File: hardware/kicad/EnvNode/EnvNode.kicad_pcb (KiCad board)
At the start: 2 copper layers, 111 x 95 mm, 38 parts, among them J1 Conn_01x02_Pin, U1 LT1963AxST-3.3, U2 ESP32-DevKitC

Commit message: Changed Value to LM3940IMP
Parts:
- U1: value LT1963AxST-3.3 -> LM3940IMP-3.3/NOPB
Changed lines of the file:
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@@
 			)
 		)
-		(property "Value" "LT1963AxST-3.3"
+		(property "Value" "LM3940IMP-3.3/NOPB"
 			(at 0 4.5 90)
 			(layer "F.Fab")

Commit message: hardware(mainboard): add board ID EEPROM for revision 0.2
Add a 24AA025E48 EEPROM to the system I2C bus on GPIO21/22.
Configure address pins A0 and A1 for address 0x50 and update the
board revision markings to Rev 0.2.
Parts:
- added U3: 24AA025E-OT, Package_TO_SOT_SMD:SOT-23-6, F.Cu at (148.1, 45.7)
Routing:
- net +3V3: track 342.1 -> 358.9 mm
- net I2C0_SDA: track 129.8 -> 146.5 mm
- net I2C0_SCL: track 118.2 -> 129.3 mm
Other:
- board text added: "${TITLE} - Rev ${REVISION}"
- board text removed: "${TITLE} - ${REVISION}"

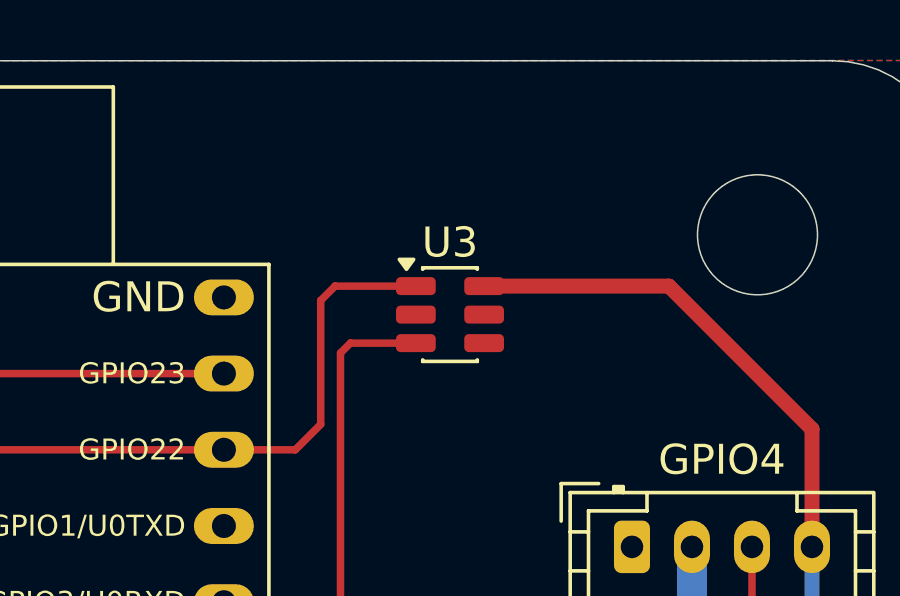
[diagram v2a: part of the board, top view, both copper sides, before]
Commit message: Change EEPROM-Package to SOT-23-6
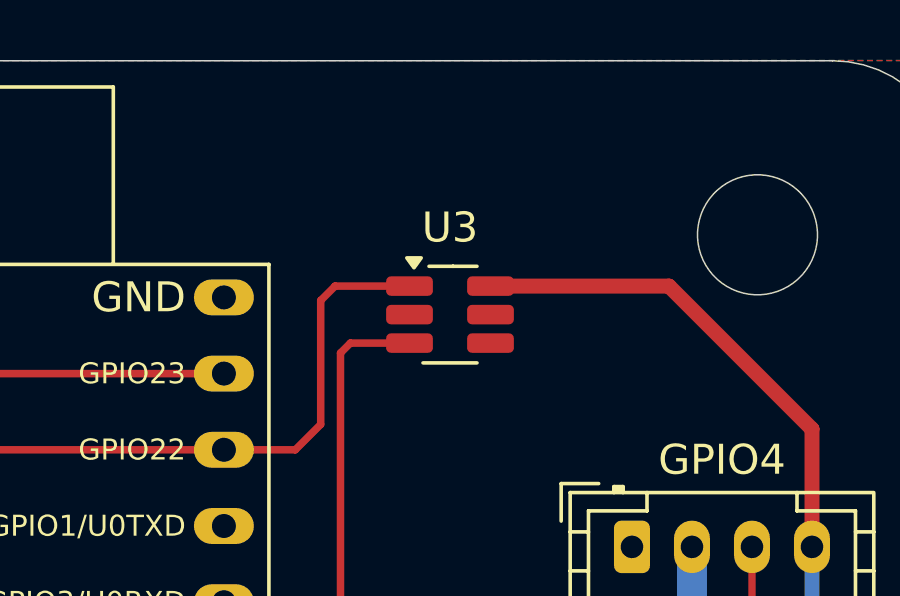
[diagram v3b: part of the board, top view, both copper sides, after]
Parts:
- U3: footprint Package_TO_SOT_SMD:SOT-23-6 -> Package_TO_SOT_SMD:SOT-23-6_Handsoldering
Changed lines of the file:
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@@
 		)
 	)
-	(footprint "Package_TO_SOT_SMD:SOT-23-6"
+	(footprint "Package_TO_SOT_SMD:SOT-23-6_Handsoldering"
 		(layer "F.Cu")
 		(at 148.09 45.7)
-		(descr "SOT, 6 Pin (JEDEC MO-178 Var AB https://www.jedec.org/document_search?search_api_views_fulltext=MO-178)")
-		(tags "SOT TO_SOT_SMD")
+		(descr "6-pin SOT-23 package, Handsoldering")
+		(tags "SOT-23-6 Handsoldering")
 		(property "Reference" "U3"
-			(at 0 -2.4 0)
+			(at 0 -2.9 0)
 			(layer "F.SilkS")
 			(effects
@@
 		)
 		(property "Value" "24AA025E-OT"
-			(at 0 2.4 0)
+			(at 0 2.9 0)
 			(layer "F.Fab")
 			(effects
@@
 		(property "Datasheet" "https://ww1.microchip.com/downloads/aemDocuments/documents/MPD/ProductDocuments/DataSheets/2-Kbit-I2C-Serial-EEPROMs-+EUI-48-or-EUI-64-Node-20002124.pdf"
 			(at 0 0 0)
+			(unlocked yes)
 			(layer "F.Fab")
 			(hide yes)
@@
 				(font
 					(size 1.27 1.27)
+					(thickness 0.15)
 				)
 			)
@@
 		(property "Description" "I2C Serial EEPROM with EUI-48 or EUI-64, 2Kb, SOT-23-6"
 			(at 0 0 0)
+			(unlocked yes)
 			(layer "F.Fab")
 			(hide yes)
@@
 				(font
 					(size 1.27 1.27)
-				)
-			)
-		)
-		(property "KiLib_Generator" "package/gullwing"
-			(at 0 0 0)
-			(layer "F.SilkS")
-			(hide yes)
-			(effects
-				(font
-					(size 1 1)
 					(thickness 0.15)
 				)
@@
 		(duplicate_pad_numbers_are_jumpers no)
 		(fp_line
-			(start -0.91 -1.56)
-			(end 0.91 -1.56)
-			(stroke
-				(width 0.12)
-				(type solid)
-			)
-			(layer "F.SilkS")
-		)
-		(fp_line
-			(start -0.91 -1.51)
-			(end -0.91 -1.56)
-			(stroke
-				(width 0.12)
-				(type solid)
-			)
-			(layer "F.SilkS")
-		)
-		(fp_line
-			(start -0.91 1.56)
-			(end -0.91 1.51)
-			(stroke
-				(width 0.12)
-				(type solid)
-			)
-			(layer "F.SilkS")
-		)
-		(fp_line
-			(start 0.91 -1.56)
-			(end 0.91 -1.51)
-			(stroke
-				(width 0.12)
-				(type solid)
-			)
-			(layer "F.SilkS")
-		)
-		(fp_line
-			(start 0.91 1.51)
-			(end 0.91 1.56)
-			(stroke
-				(width 0.12)
-				(type solid)
-			)
-			(layer "F.SilkS")
-		)
-		(fp_line
-			(start 0.91 1.56)
-			(end -0.91 1.56)
+			(start -0.9 1.61)
+			(end 0.9 1.61)
+			(stroke
+				(width 0.12)
+				(type solid)
+			)
+			(layer "F.SilkS")
+		)
+		(fp_line
+			(start 0.1 -1.61)
+			(end -0.7 -1.61)
+			(stroke
+				(width 0.12)
+				(type solid)
+			)
+			(layer "F.SilkS")
+		)
+		(fp_line
+			(start 0.1 -1.61)
+			(end 0.9 -1.61)
 			(stroke
 				(width 0.12)
@@
 		(fp_poly
 			(pts
-				(xy -1.45 -1.51) (xy -1.69 -1.84) (xy -1.21 -1.84)
+				(xy -1.2 -1.56) (xy -1.44 -1.89) (xy -0.96 -1.89) (xy -1.2 -1.56)
 			)
 			(stroke
@@
 		)
 		(fp_line
-			(start -2.05 -1.5)
-			(end -1.05 -1.5)
-			(stroke
-				(width 0.05)
-				(type solid)
-			)
-			(layer "F.CrtYd")
-		)
-		(fp_line
-			(start -2.05 1.5)
-			(end -2.05 -1.5)
-			(stroke
-				(width 0.05)
-				(type solid)
-			)
-			(layer "F.CrtYd")
-		)
-		(fp_line
-			(start -1.05 -1.7)
-			(end 1.05 -1.7)
-			(stroke
-				(width 0.05)
-				(type solid)
-			)
-			(layer "F.CrtYd")
-		)
-		(fp_line
-			(start -1.05 -1.5)
-			(end -1.05 -1.7)
-			(stroke
-				(width 0.05)
-				(type solid)
-			)
-			(layer "F.CrtYd")
-		)
-		(fp_line
-			(start -1.05 1.5)
-			(end -2.05 1.5)
-			(stroke
-				(width 0.05)
-				(type solid)
-			)
-			(layer "F.CrtYd")
-		)
-		(fp_line
-			(start -1.05 1.7)
-			(end -1.05 1.5)
-			(stroke
-				(width 0.05)
-				(type solid)
-			)
-			(layer "F.CrtYd")
-		)
-		(fp_line
-			(start 1.05 -1.7)
-			(end 1.05 -1.5)
-			(stroke
-				(width 0.05)
-				(type solid)
-			)
-			(layer "F.CrtYd")
-		)
-		(fp_line
-			(start 1.05 -1.5)
-			(end 2.05 -1.5)
-			(stroke
-				(width 0.05)
-				(type solid)
-			)
-			(layer "F.CrtYd")
-		)
-		(fp_line
-			(start 1.05 1.5)
-			(end 1.05 1.7)
-			(stroke
-				(width 0.05)
-				(type solid)
-			)
-			(layer "F.CrtYd")
-		)
-		(fp_line
-			(start 1.05 1.7)
-			(end -1.05 1.7)
-			(stroke
-				(width 0.05)
-				(type solid)
-			)
-			(layer "F.CrtYd")
-		)
-		(fp_line
-			(start 2.05 -1.5)
-			(end 2.05 1.5)
-			(stroke
-				(width 0.05)
-				(type solid)
-			)
-			(layer "F.CrtYd")
-		)
-		(fp_line
-			(start 2.05 1.5)
-			(end 1.05 1.5)
-			(stroke
-				(width 0.05)
-				(type solid)
-			)
-			(layer "F.CrtYd")
-		)
-		(fp_poly
-			(pts
-				(xy -0.4 -1.45) (xy 0.8 -1.45) (xy 0.8 1.45) (xy -0.8 1.45) (xy -0.8 -1.05)
-			)
-			(stroke
-				(width 0.1)
-				(type solid)
-			)
-			(fill no)
+			(start -2.4 -1.8)
+			(end 2.4 -1.8)
+			(stroke
+				(width 0.05)
+				(type solid)
+			)
+			(layer "F.CrtYd")
+		)
+		(fp_line
+			(start -2.4 1.8)
+			(end -2.4 -1.8)
+			(stroke
+				(width 0.05)
+				(type solid)
+			)
+			(layer "F.CrtYd")
+		)
+		(fp_line
+			(start 2.4 -1.8)
+			(end 2.4 1.8)
+			(stroke
+				(width 0.05)
+				(type solid)
+			)
+			(layer "F.CrtYd")
+		)
+		(fp_line
+			(start 2.4 1.8)
+			(end -2.4 1.8)
+			(stroke
+				(width 0.05)
+				(type solid)
+			)
+			(layer "F.CrtYd")
+		)
+		(fp_line
+			(start -0.9 -0.9)
+			(end -0.9 1.55)
+			(stroke
+				(width 0.1)
+				(type solid)
+			)
+			(layer "F.Fab")
+		)
+		(fp_line
+			(start -0.9 -0.9)
+			(end -0.25 -1.55)
+			(stroke
+				(width 0.1)
+				(type solid)
+			)
+			(layer "F.Fab")
+		)
+		(fp_line
+			(start 0.9 -1.55)
+			(end -0.25 -1.55)
+			(stroke
+				(width 0.1)
+				(type solid)
+			)
+			(layer "F.Fab")
+		)
+		(fp_line
+			(start 0.9 -1.55)
+			(end 0.9 1.55)
+			(stroke
+				(width 0.1)
+				(type solid)
+			)
+			(layer "F.Fab")
+		)
+		(fp_line
+			(start 0.9 1.55)
+			(end -0.9 1.55)
+			(stroke
+				(width 0.1)
+				(type solid)
+			)
 			(layer "F.Fab")
 		)
@@
 			(effects
 				(font
-					(size 0.72 0.72)
-					(thickness 0.11)
+					(size 0.5 0.5)
+					(thickness 0.075)
 				)
 			)
 		)
 		(pad "1" smd roundrect
-			(at -1.1375 -0.95)
-			(size 1.325 0.6)
+			(at -1.35 -0.95)
+			(size 1.56 0.65)
 			(layers "F.Cu" "F.Mask" "F.Paste")
 			(roundrect_rratio 0.25)
@@
 		)
 		(pad "2" smd roundrect
-			(at -1.1375 0)
-			(size 1.325 0.6)
+			(at -1.35 0)
+			(size 1.56 0.65)
 			(layers "F.Cu" "F.Mask" "F.Paste")
 			(roundrect_rratio 0.25)
@@
 		)
 		(pad "3" smd roundrect
-			(at -1.1375 0.95)
-			(size 1.325 0.6)
+			(at -1.35 0.95)
+			(size 1.56 0.65)
 			(layers "F.Cu" "F.Mask" "F.Paste")
 			(roundrect_rratio 0.25)
@@
 		)
 		(pad "4" smd roundrect
-			(at 1.1375 0.95)
-			(size 1.325 0.6)
+			(at 1.35 0.95)
+			(size 1.56 0.65)
 			(layers "F.Cu" "F.Mask" "F.Paste")
 			(roundrect_rratio 0.25)
@@
 		)
 		(pad "5" smd roundrect
-			(at 1.1375 0)
-			(size 1.325 0.6)
+			(at 1.35 0)
+			(size 1.56 0.65)
 			(layers "F.Cu" "F.Mask" "F.Paste")
 			(roundrect_rratio 0.25)
@@
 		)
 		(pad "6" smd roundrect
-			(at 1.1375 -0.95)
-			(size 1.325 0.6)
-			(layers "F.Cu" "F.Mask" "F.Paste")
-			(roundrect_rratio 0.25)
+			(at 1.35 -0.95)
+			(size 1.56 0.65)
+			(layers "F.Cu" "F.Mask" "F.Paste")
+			(roundrect_rratio 0.25)

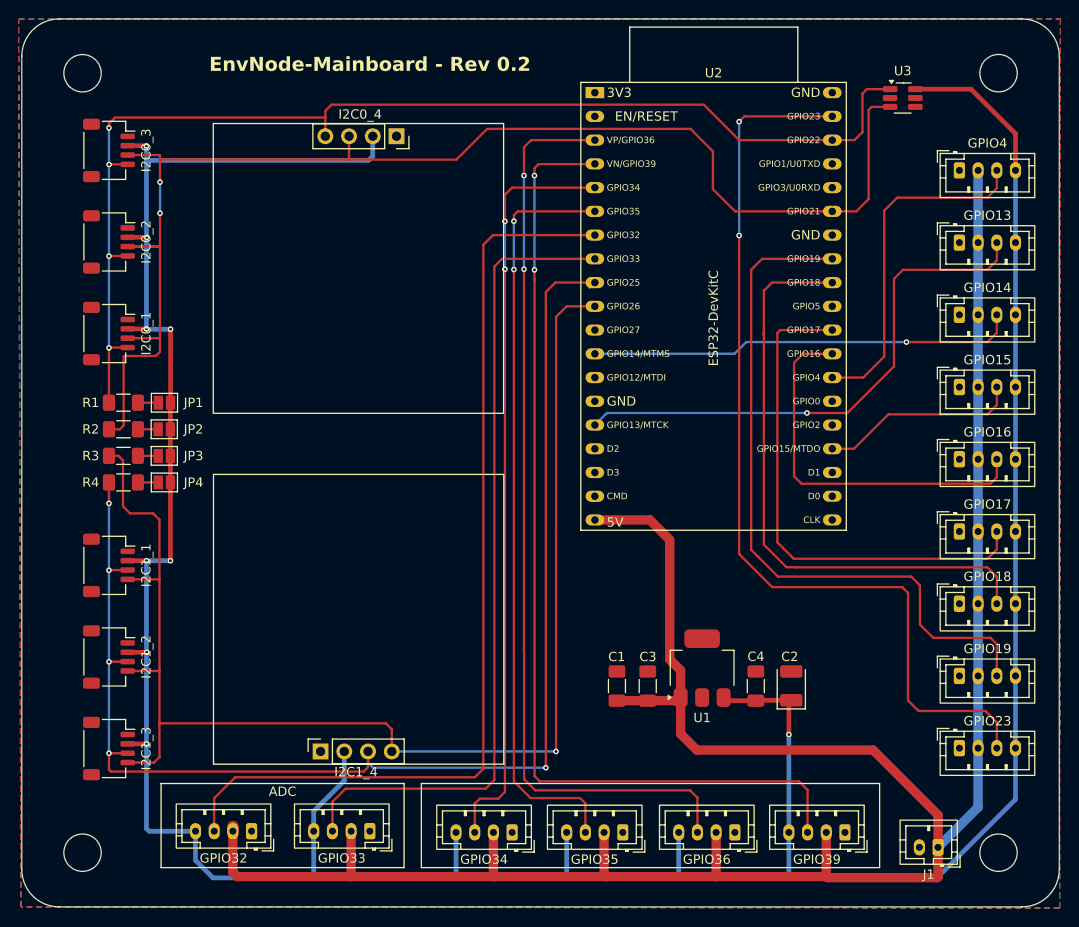
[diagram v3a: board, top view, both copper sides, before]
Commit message: Fixed Footprint-Assignments, DesignBlocks
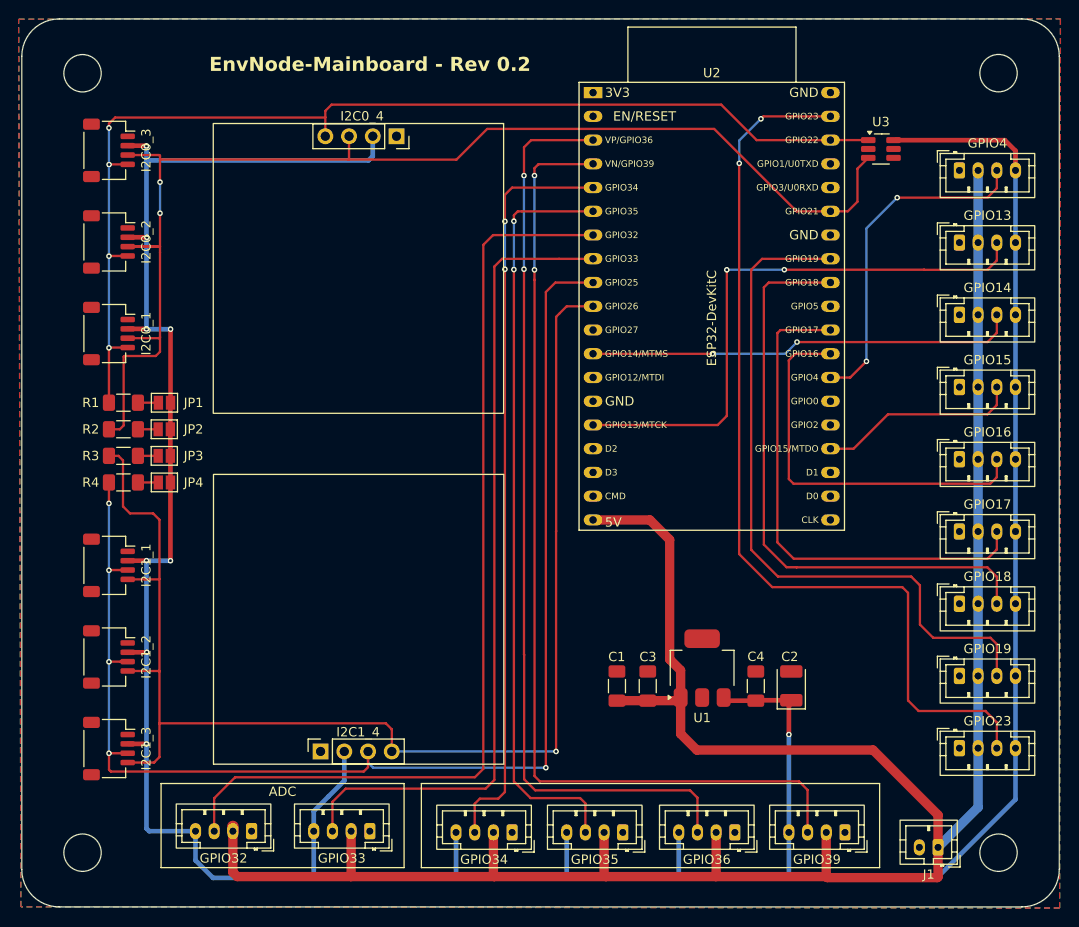
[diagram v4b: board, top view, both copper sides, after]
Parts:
- I2C0_4, I2C1_4: footprint EnvNode:QWIIC_PinSocket_1x04_P2.54mm_Vertical -> EnvNode-Footprints:QWIIC_PinSocket_1x04_P2.54mm_Vertical
- moved U3 5.93 mm to (145.8, 51.2)
- moved U2 0.19 mm to (115.0, 45.1)
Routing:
- net I2C0_SDA: track 146.5 -> 136.0 mm
- net I2C0_SCL: track 129.3 -> 122.3 mm
- net GPIO13: track 57.7 -> 61.4 mm, vias 1 -> 2
- net GPIO16: track 40.9 -> 42.3 mm
- net +3V3: track 358.9 -> 357.5 mm
- net GPIO23: track 101.0 -> 99.8 mm
- net GPIO4: track 37.0 -> 36.2 mm, vias 0 -> 2
- net I2C1_SDA: track 145.0 -> 144.2 mm
- net GPIO14: vias 1 -> 2
